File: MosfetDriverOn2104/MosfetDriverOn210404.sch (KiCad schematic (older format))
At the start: 74 parts, among them J1 Screw_Terminal_01x02, J10 CROSS CONN, J11 servo hdr, J12 motor, J2 AVR-ISP-6, J3 I2C HDR, J4 I2C HDR, J5 UART HDR, J6 I2C HDR, J7 5V HDR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

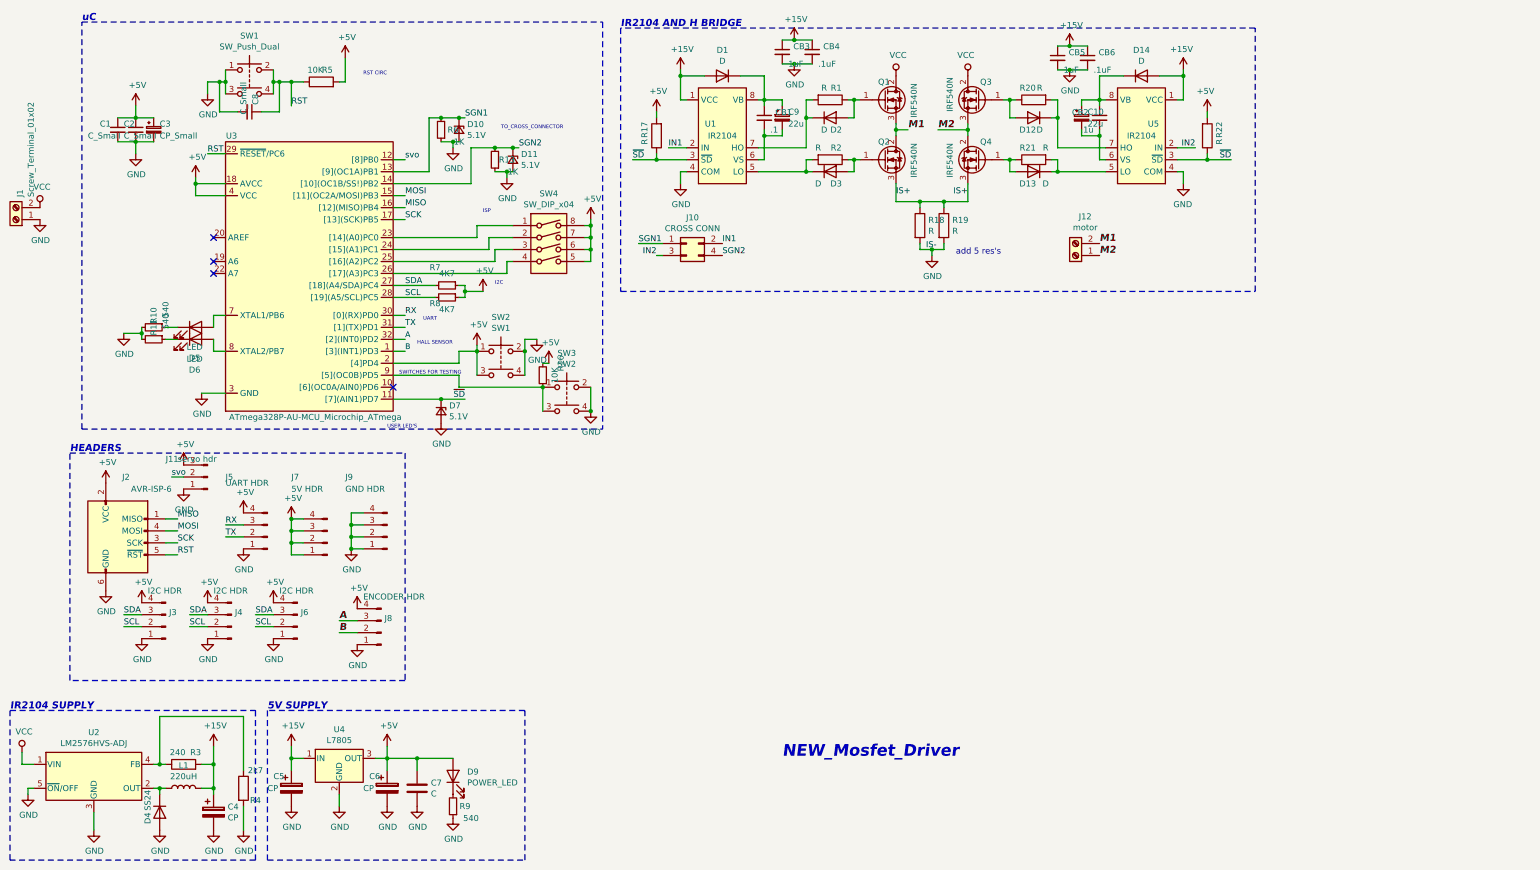
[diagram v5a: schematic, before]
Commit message: Started organising schematic
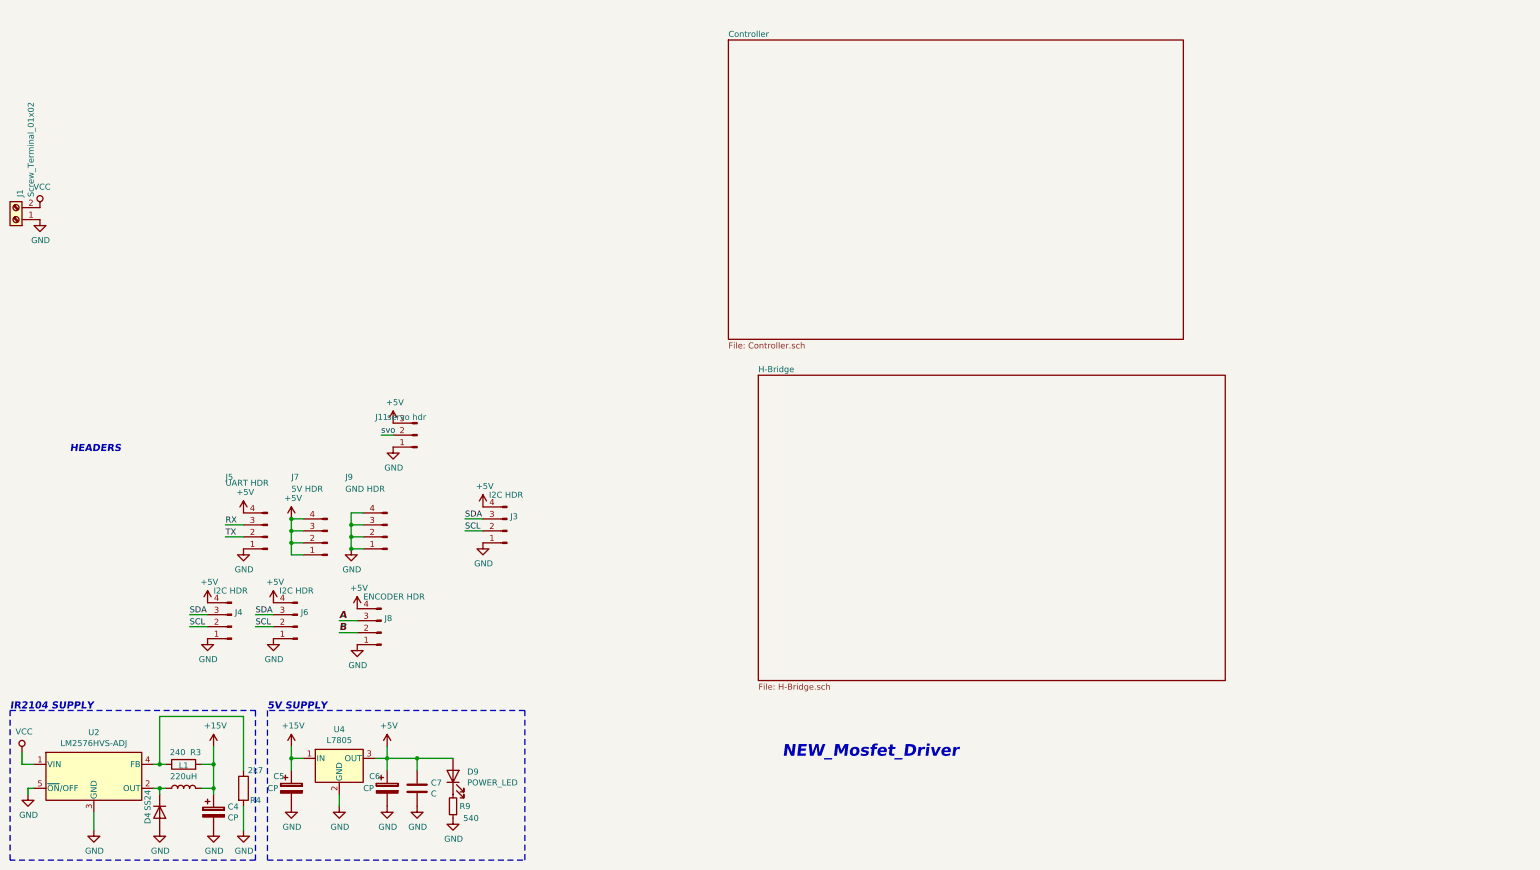
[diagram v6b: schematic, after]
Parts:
- removed C1, C2, C8: C_Small, Capacitor_SMD:C_0805_2012Metric, symbol Device:C_Small
- removed C10, C9: 22u, Capacitor_SMD:C_0805_2012Metric, symbol Device:CP_Small
- removed C3: CP_Small, Capacitor_SMD:CP_Elec_5x4.4, symbol Device:CP_Small
- removed CB1: .1, Capacitor_SMD:C_0805_2012Metric, symbol Device:C_Small
- removed CB2: .1u, Capacitor_SMD:C_0805_2012Metric, symbol Device:C_Small
- removed CB3, CB5: 1uF, Capacitor_SMD:C_0805_2012Metric, symbol Device:C_Small
- removed CB4, CB6: .1uF, Capacitor_SMD:C_0805_2012Metric, symbol Device:C_Small
- removed D1, D12, D13, D14, D2, D3: D, Diode_SMD:D_SMA, symbol Device:D
- removed D10, D11: 5.1V, Diodes_SMD:D_SMA, symbol Device:D_Zener_Small
- removed D5, D6: LED, LED_SMD:LED_0805_2012Metric, symbol Device:LED
- removed D7: 5.1V, LED_SMD:LED_0805_2012Metric, symbol Device:D_Zener_Small
- removed J10: CROSS CONN, Connector_PinHeader_2.54mm:PinHeader_1x04_P2.54mm_Vertical, symbol Connector_Generic:Conn_02x02_Odd_Even
- removed J12: motor, TerminalBlock:TerminalBlock_Altech_AK300-2_P5.00mm, symbol Connector:Screw_Terminal_01x02
- removed J2: AVR-ISP-6, Connector_PinHeader_2.54mm:PinHeader_1x04_P2.54mm_Vertical, symbol Connector:AVR-ISP-6
- removed Q1, Q2, Q3, Q4: IRF540N, Footprints:TO220_HS_SCREW, symbol Transistor_FET:IRF540N
- removed R1, R17, R2, R20, R21, R22: R, Resistor_SMD:R_0805_2012Metric, symbol Device:R
- removed R10, R11: 540, Resistor_SMD:R_0805_2012Metric, symbol Device:R_Small
- removed R13, R6: 1K, Resistor_SMD:R_0805_2012Metric, symbol Device:R_Small
- removed R16: 10K, Resistor_SMD:R_0805_2012Metric, symbol Device:R_Small
- removed R18, R19: R, Resistor_SMD:R_1206_3216Metric, symbol Device:R
- removed R5: 10K, Resistor_SMD:R_0805_2012Metric, symbol Device:R
- removed R7: 4K7, Resistor_SMD:R_0805_2012Metric, symbol Device:R_Small
- removed R8: 4K7, Resistors_SMD:R_0805, symbol Device:R_Small
- removed SW1: SW_Push_Dual, Button_Switch_THT:SW_PUSH_6mm, symbol Switch:SW_Push_Dual
- removed SW2: SW1, Button_Switch_THT:SW_PUSH_6mm, symbol Switch:SW_Push_Dual
- removed SW3: SW2, Button_Switch_THT:SW_PUSH_6mm, symbol Switch:SW_Push_Dual
- removed SW4: SW_DIP_x04, Button_Switch_THT:SW_DIP_SPSTx04_Slide_9.78x12.34mm_W7.62mm_P2.54mm, symbol Switch:SW_DIP_x04
- removed U1, U5: IR2104, Package_DIP:DIP-8_W7.62mm_Socket_LongPads, symbol Driver_FET:IR2104
- removed U3: ATmega328P-AU-MCU_Microchip_ATmega, Package_QFP:TQFP-32_7x7mm_P0.8mm, symbol MosfetDriverOn210404-rescue:ATmega328P-AU-MCU_Microchip_ATmega
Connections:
- no-connect marks 4 -> 0
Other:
- note removed: "HALL SENSOR\n"
- note removed: "I2C\n"
- note removed: "IR2104 AND H BRIDGE"
- note removed: "ISP"
- note removed: "RST CIRC"
- note removed: "SWITCHES FOR TESTING\n"
- note removed: "TO_CROSS_CONNECTOR"
- note removed: "UART\n"
- note removed: "USER LED'S\n"
- note removed: "add 5 res's"
- note removed: "uC"
- moved on the sheet: J11, J3

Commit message: Completed Hirarcheial Sch, fixes #9
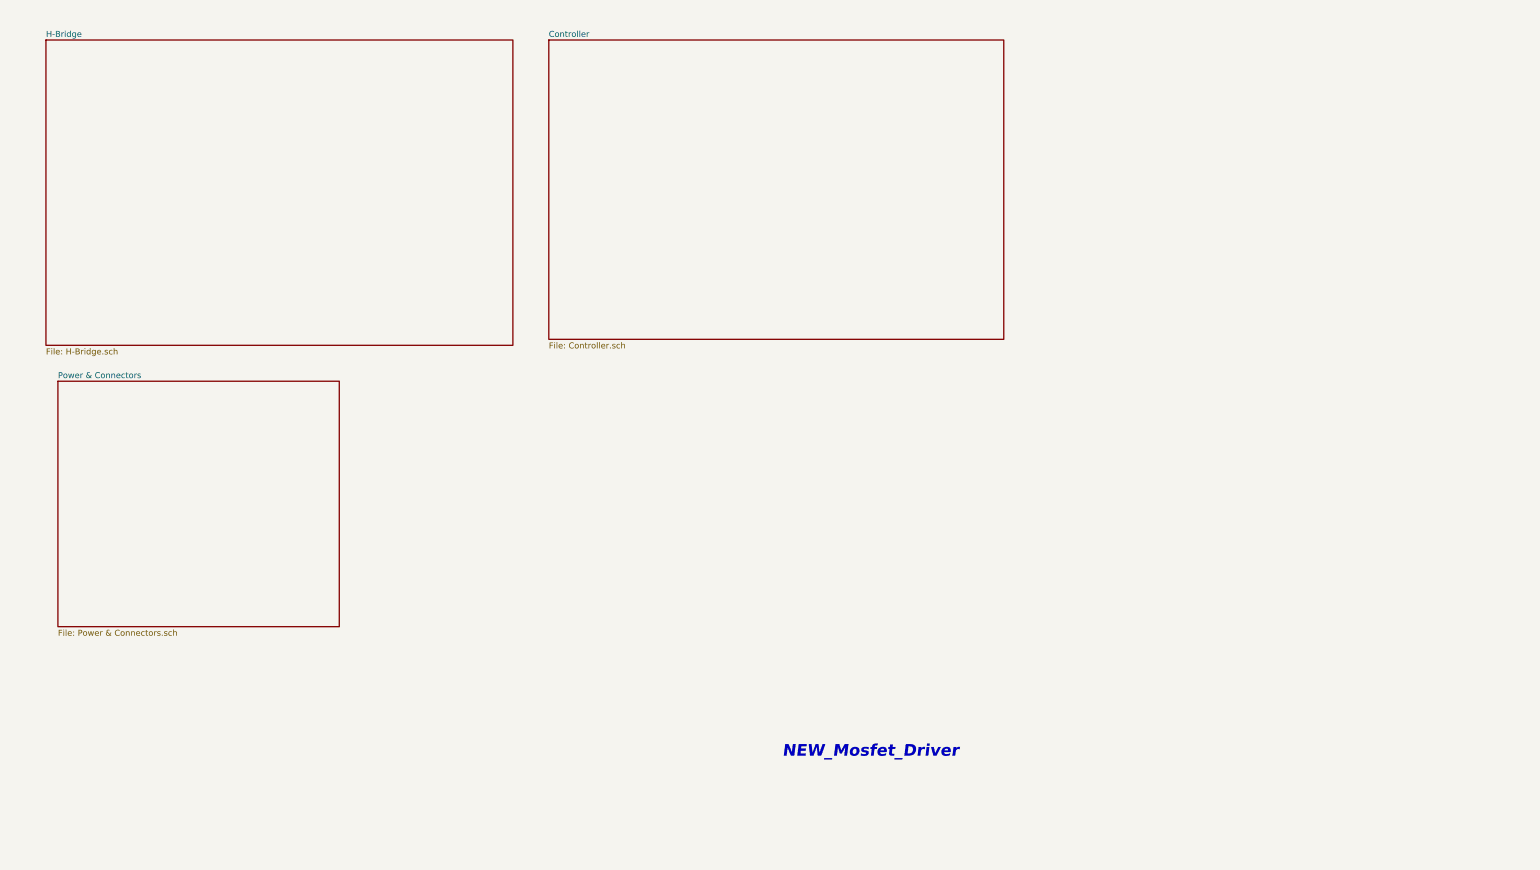
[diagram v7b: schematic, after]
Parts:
- removed C4: CP, Capacitor_SMD:CP_Elec_6.3x5.7, symbol Device:CP
- removed C5, C6: CP, Capacitor_SMD:CP_Elec_5x5.4, symbol Device:CP
- removed C7: C, Capacitor_SMD:C_0805_2012Metric, symbol Device:C
- removed D4: SS24, Diode_SMD:D_SMA, symbol Device:D
- removed D9: POWER_LED, LED_SMD:LED_0805_2012Metric, symbol Device:LED
- removed J1: Screw_Terminal_01x02, TerminalBlock:TerminalBlock_Altech_AK300-2_P5.00mm, symbol Connector:Screw_Terminal_01x02
- removed J11: servo hdr, TerminalBlock:TerminalBlock_Altech_AK300-3_P5.00mm, symbol Connector:Conn_01x03_Male
- removed J3, J4, J6: I2C HDR, Connector_PinHeader_2.54mm:PinHeader_1x04_P2.54mm_Vertical, symbol Connector:Conn_01x04_Male
- removed J5: UART HDR, Connector_PinHeader_2.54mm:PinHeader_1x04_P2.54mm_Vertical, symbol Connector:Conn_01x04_Male
- removed J7: 5V HDR, Connector_PinHeader_2.54mm:PinHeader_1x04_P2.54mm_Vertical, symbol Connector:Conn_01x04_Male
- removed J8: ENCODER HDR, Connector_PinHeader_2.54mm:PinHeader_1x04_P2.54mm_Vertical, symbol Connector:Conn_01x04_Male
- removed J9: GND HDR, Connector_PinHeader_2.54mm:PinHeader_1x04_P2.54mm_Vertical, symbol Connector:Conn_01x04_Male
- removed L1: 220uH, Inductor_SMD:L_12x12mm_H6mm, symbol Device:L
- removed R3: 240, Resistor_SMD:R_0805_2012Metric, symbol Device:R
- removed R4: 2k7, Resistor_SMD:R_0805_2012Metric, symbol Device:R
- removed R9: 540, Resistor_SMD:R_0805_2012Metric, symbol Device:R_Small
- removed U2: LM2576HVS-ADJ, Package_TO_SOT_SMD:TO-263-5_TabPin3, symbol Regulator_Switching:LM2576HVS-ADJ
- removed U4: L7805, symbol Regulator_Linear:L7805
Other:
- note removed: "5V SUPPLY"
- note removed: "HEADERS"
- note removed: "IR2104 SUPPLY"
